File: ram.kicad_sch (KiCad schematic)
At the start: 26 parts, among them U16 SIMM, U17 74LS08, U18 74LS74, U19 74F00, U32 74LS139, U34 74LS244, U35 74LS244

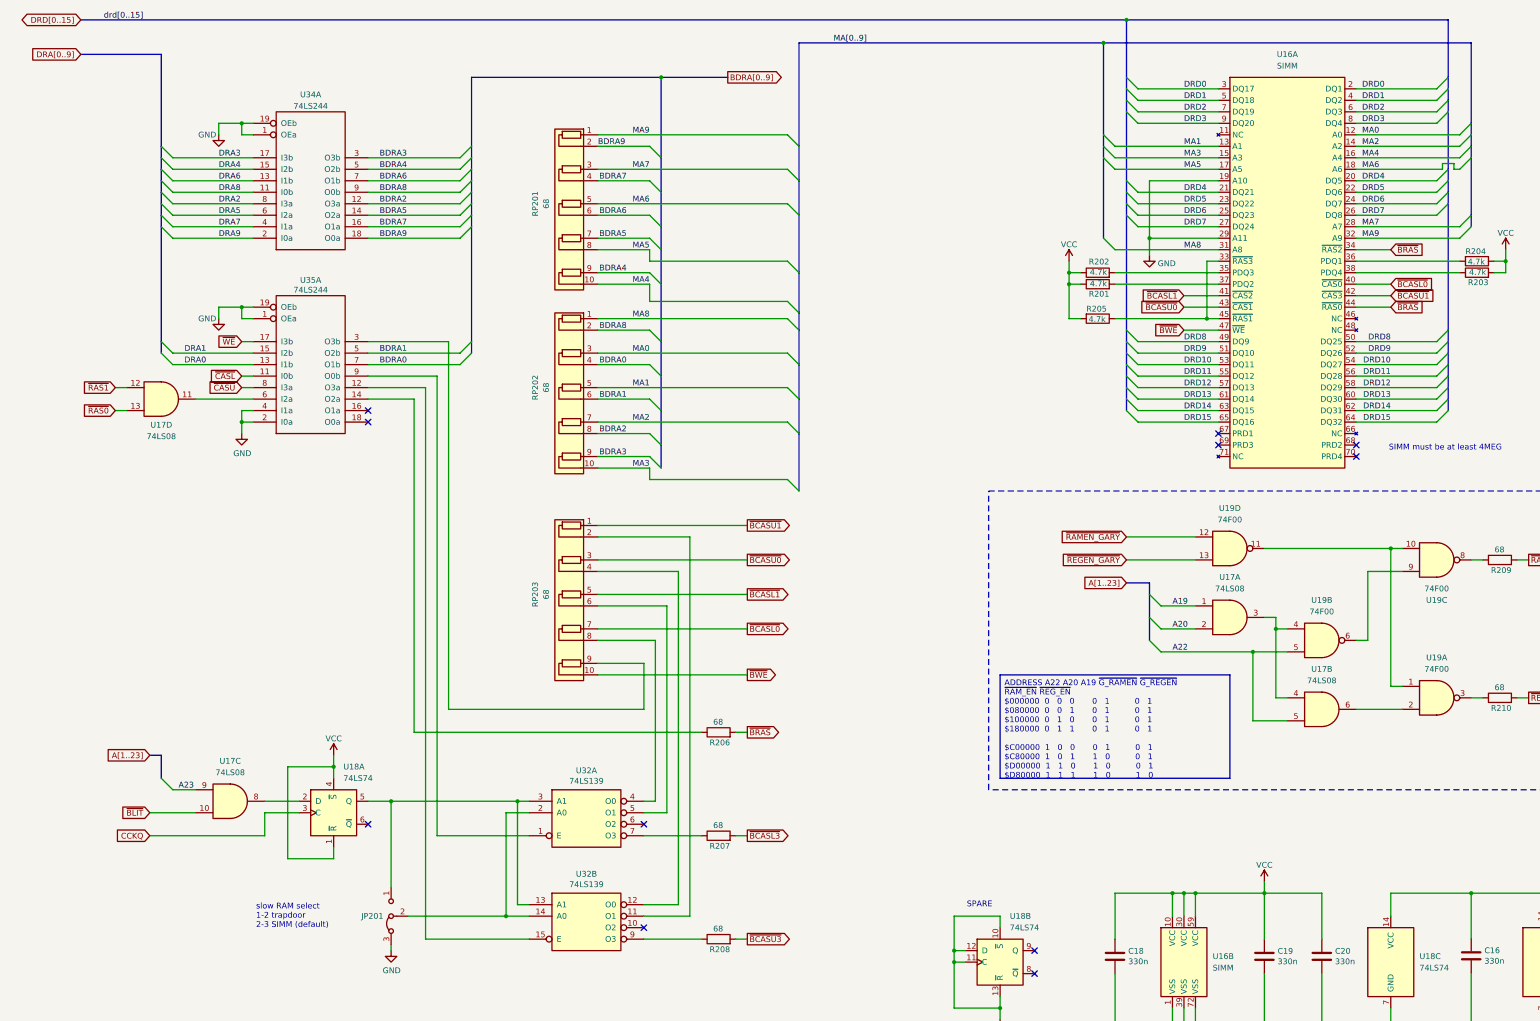
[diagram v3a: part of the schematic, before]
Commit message: routing SIMM
work in progress
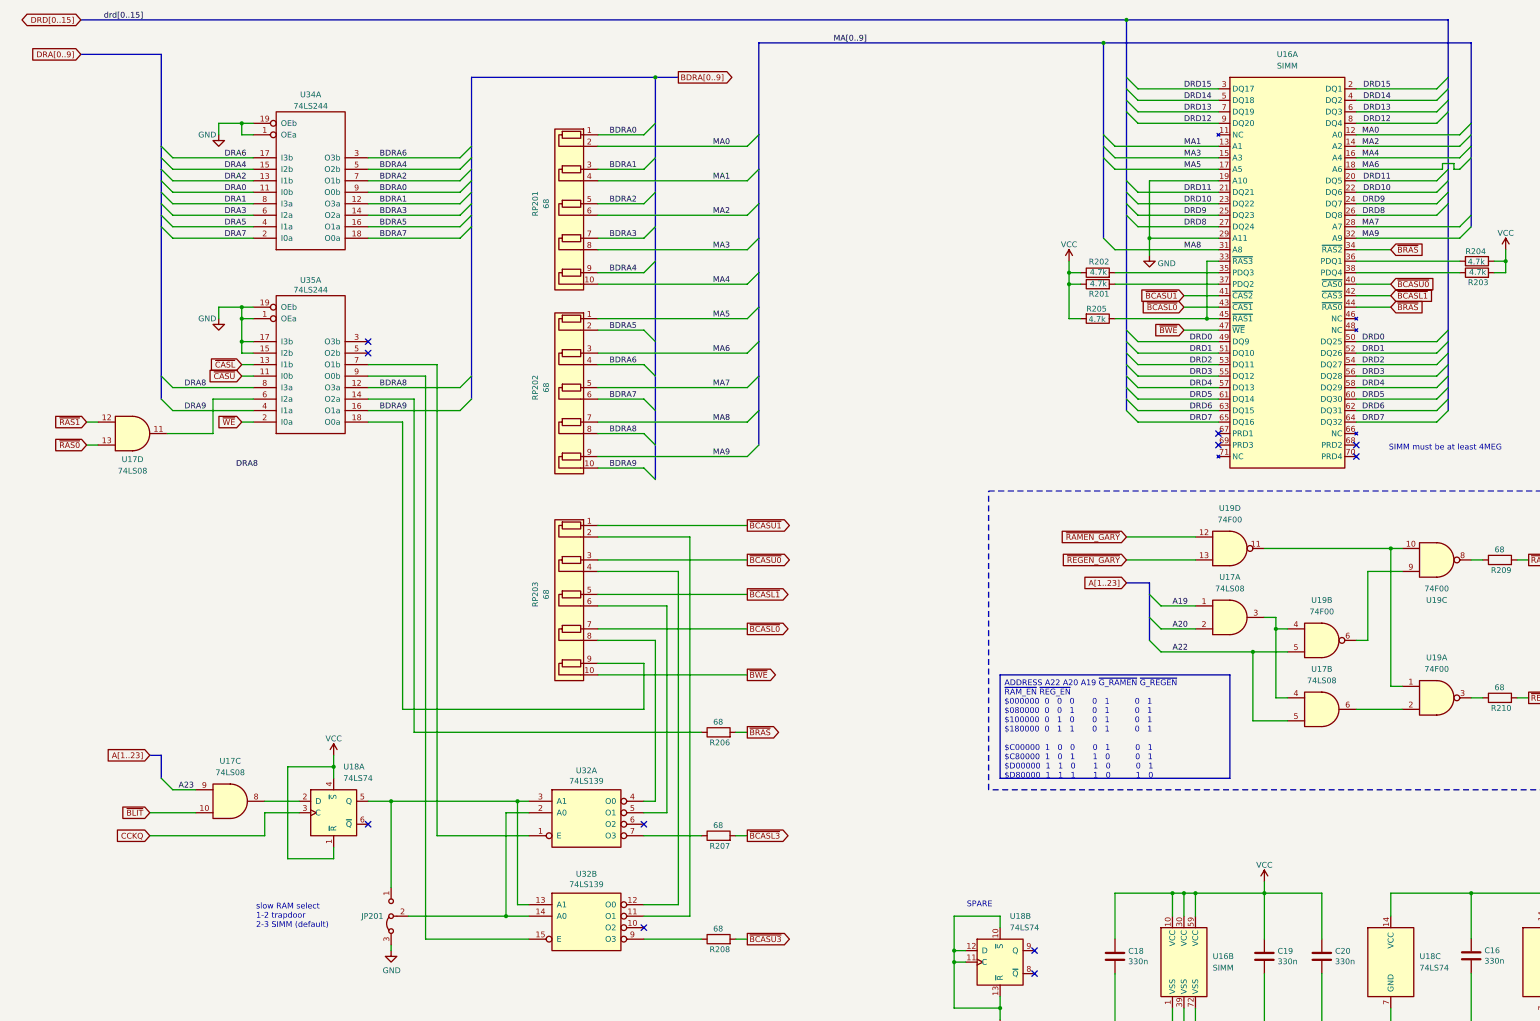
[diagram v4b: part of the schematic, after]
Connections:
- net BDRA0: now also RP201.1 (R1.1), U34.9 (O0b); no longer RP202.4 (R2.2), U35.7 (O1b)
- net BDRA1: now also RP201.3 (R2.1), U34.12 (O3a); no longer RP202.6 (R3.2), U35.5 (O2b)
- net BDRA2: now also RP201.5 (R3.1), U34.7 (O1b); no longer RP202.8 (R4.2), U34.12 (O3a)
- net BDRA3: now also RP201.7 (R4.1), U34.14 (O2a); no longer RP202.9 (R5.1), U34.3 (O3b)
- net BDRA5: now also RP202.2 (R1.2), U34.16 (O1a); no longer RP201.7 (R4.1), U34.14 (O2a)
- net BDRA6: now also RP202.4 (R2.2), U34.3 (O3b); no longer RP201.6 (R3.2), U34.7 (O1b)
- net BDRA7: now also RP202.6 (R3.2), U34.18 (O0a); no longer RP201.4 (R2.2), U34.16 (O1a)
- net BDRA8: now also RP202.8 (R4.2), U35.12 (O3a); no longer RP202.2 (R1.2), U34.9 (O0b)
- net BDRA9: now also RP202.10 (R5.2), U35.16 (O1a); no longer RP201.2 (R1.2), U34.18 (O0a)
- net DRA0: now also U34.11 (I0b); no longer U35.13 (I1b)
- net DRA1: now also U34.8 (I3a); no longer U35.15 (I2b)
- net DRA2: now also U34.13 (I1b); no longer U34.8 (I3a)
- net DRA3: now also U34.6 (I2a); no longer U34.17 (I3b)
- net DRA5: now also U34.4 (I1a); no longer U34.6 (I2a)
- net DRA6: now also U34.17 (I3b); no longer U34.13 (I1b)
- net DRA7: now also U34.2 (I0a); no longer U34.4 (I1a)
- net DRA8: now also U35.8 (I3a); no longer U34.11 (I0b)
- net DRA9: now also U35.4 (I1a); no longer U34.2 (I0a)
- net DRD0: now also U16.49 (DQ9), U16.50 (DQ25); no longer U16.2 (DQ1), U16.3 (DQ17)
- net DRD1: now also U16.51 (DQ10), U16.52 (DQ26); no longer U16.4 (DQ2), U16.5 (DQ18)
- net DRD10: now also U16.22 (DQ6), U16.23 (DQ22); no longer U16.53 (DQ11), U16.54 (DQ27)
- net DRD11: now also U16.20 (DQ5), U16.21 (DQ21); no longer U16.55 (DQ12), U16.56 (DQ28)
- net DRD12: now also U16.8 (DQ4), U16.9 (DQ20); no longer U16.57 (DQ13), U16.58 (DQ29)
- net DRD13: now also U16.6 (DQ3), U16.7 (DQ19); no longer U16.60 (DQ30), U16.61 (DQ14)
- net DRD14: now also U16.4 (DQ2), U16.5 (DQ18); no longer U16.62 (DQ31), U16.63 (DQ15)
- net DRD15: now also U16.2 (DQ1), U16.3 (DQ17); no longer U16.64 (DQ32), U16.65 (DQ16)
- net DRD2: now also U16.53 (DQ11), U16.54 (DQ27); no longer U16.6 (DQ3), U16.7 (DQ19)
- net DRD3: now also U16.55 (DQ12), U16.56 (DQ28); no longer U16.8 (DQ4), U16.9 (DQ20)
- net DRD4: now also U16.57 (DQ13), U16.58 (DQ29); no longer U16.20 (DQ5), U16.21 (DQ21)
- net DRD5: now also U16.60 (DQ30), U16.61 (DQ14); no longer U16.22 (DQ6), U16.23 (DQ22)
- net DRD6: now also U16.62 (DQ31), U16.63 (DQ15); no longer U16.24 (DQ7), U16.25 (DQ23)
- net DRD7: now also U16.64 (DQ32), U16.65 (DQ16); no longer U16.26 (DQ8), U16.27 (DQ24)
- net DRD8: now also U16.26 (DQ8), U16.27 (DQ24); no longer U16.49 (DQ9), U16.50 (DQ25)
- net DRD9: now also U16.24 (DQ7), U16.25 (DQ23); no longer U16.51 (DQ10), U16.52 (DQ26)
- net GND: now also U35.15 (I2b), U35.17 (I3b); no longer U35.2 (I0a), U35.4 (I1a)
- net MA0: now also RP201.2 (R1.2); no longer RP202.3 (R2.1)
- net MA1: now also RP201.4 (R2.2); no longer RP202.5 (R3.1)
- net MA2: now also RP201.6 (R3.2); no longer RP202.7 (R4.1)
- net MA3: now also RP201.8 (R4.2); no longer RP202.10 (R5.2)
- net MA5: now also RP202.1 (R1.1); no longer RP201.8 (R4.2)
- net MA6: now also RP202.3 (R2.1); no longer RP201.5 (R3.1)
- net MA7: now also RP202.5 (R3.1); no longer RP201.3 (R2.1)
- net MA8: now also RP202.7 (R4.1); no longer RP202.1 (R1.1)
- net MA9: now also RP202.9 (R5.1); no longer RP201.1 (R1.1)
- net ~{BCASL0}: now also U16.43 (~{CAS1}); no longer U16.40 (~{CAS0})
- net ~{BCASL1}: now also U16.42 (~{CAS3}); no longer U16.41 (~{CAS2})
- net ~{BCASU0}: now also U16.40 (~{CAS0}); no longer U16.43 (~{CAS1})
- net ~{BCASU1}: now also U16.41 (~{CAS2}); no longer U16.42 (~{CAS3})
- net ~{CASL}: now also U35.13 (I1b); no longer U35.11 (I0b)
- net ~{CASU}: now also U35.11 (I0b); no longer U35.8 (I3a)
- net ~{WE}: now also U35.2 (I0a); no longer U35.17 (I3b)
- net at U32.1 (E): now also U35.7 (O1b); no longer U35.9 (O0b)
- net at U32.15 (E): now also U35.9 (O0b); no longer U35.12 (O3a)
- net at U35.18 (O0a): now also RP203.9 (R5.1)
- net at U35.3 (O3b): no longer RP203.9 (R5.1)
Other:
- moved on the sheet: U17D

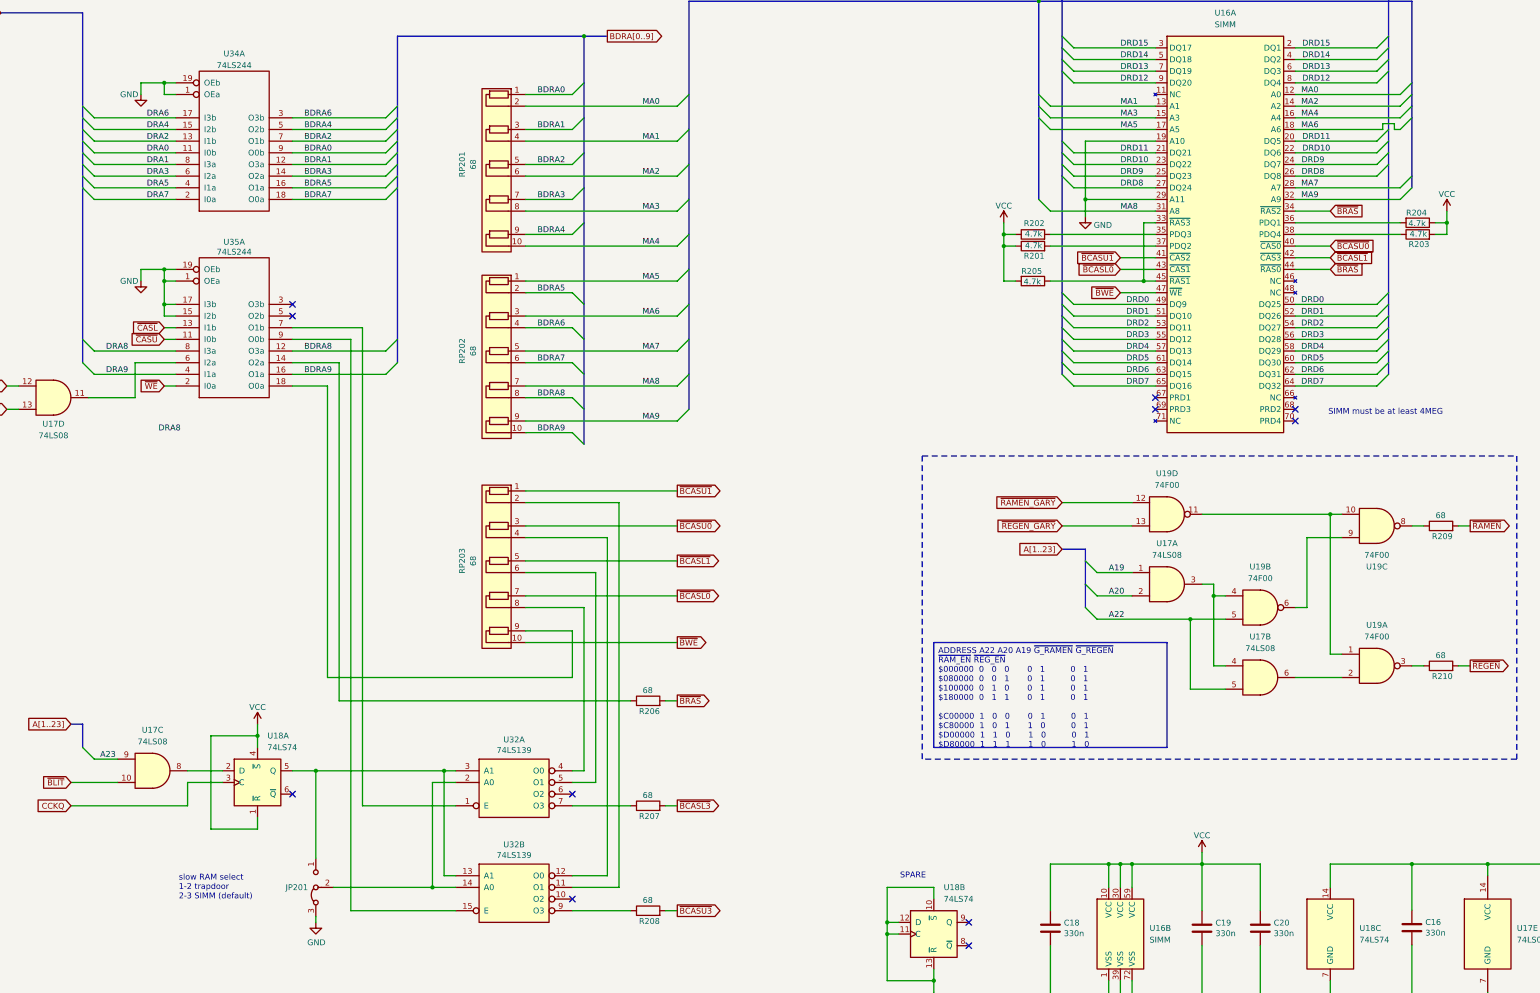
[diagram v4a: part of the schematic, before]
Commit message: changed wiring of pullups, simplified SIMM parity pullups
Routed more nets. Slowly getting there. WIP
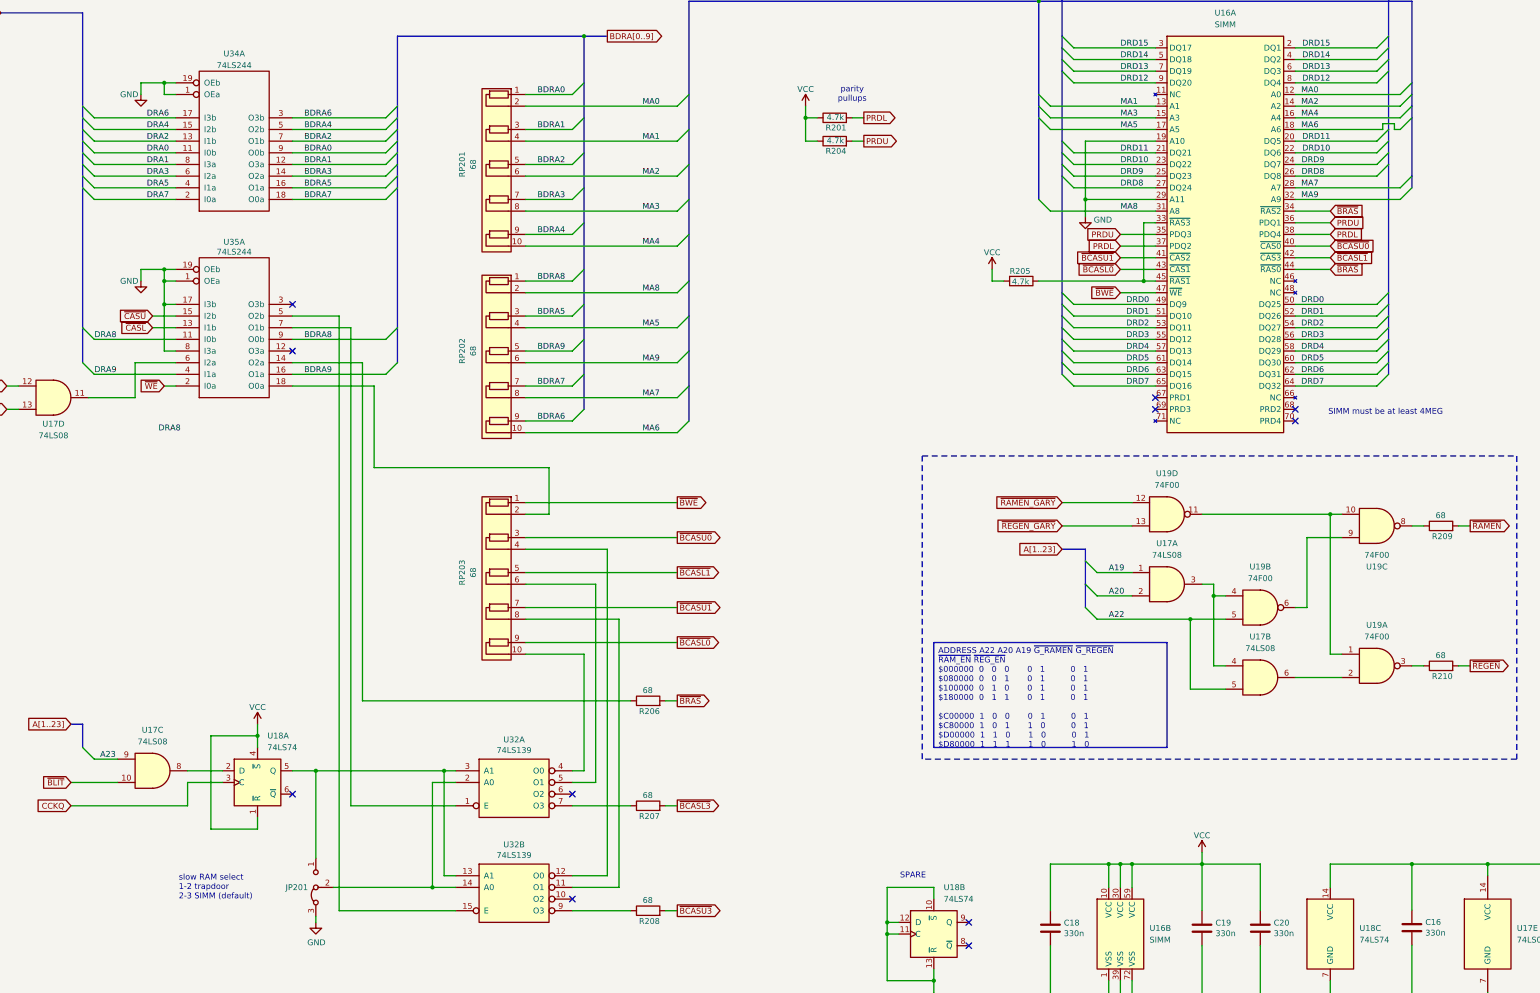
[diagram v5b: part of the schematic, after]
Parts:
- removed R202, R203: 4.7k, Raemixx500:R_Axial_DIN0309_L9.0mm_D3.2mm_P12.70mm_Horizontal, symbol Device:R
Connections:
- net BDRA5: now also RP202.3 (R2.1); no longer RP202.2 (R1.2)
- net BDRA6: now also RP202.9 (R5.1); no longer RP202.4 (R2.2)
- net BDRA7: now also RP202.7 (R4.1); no longer RP202.6 (R3.2)
- net BDRA8: now also RP202.1 (R1.1), U35.9 (O0b); no longer RP202.8 (R4.2), U35.12 (O3a)
- net BDRA9: now also RP202.5 (R3.1); no longer RP202.10 (R5.2)
- net DRA8: now also U35.11 (I0b); no longer U35.8 (I3a)
- net GND: now also U35.8 (I3a); no longer U35.15 (I2b)
- net MA5: now also RP202.4 (R2.2); no longer RP202.1 (R1.1)
- net MA6: now also RP202.10 (R5.2); no longer RP202.3 (R2.1)
- net MA7: now also RP202.8 (R4.2); no longer RP202.5 (R3.1)
- net MA8: now also RP202.2 (R1.2); no longer RP202.7 (R4.1)
- net MA9: now also RP202.6 (R3.2); no longer RP202.9 (R5.1)
- net ~{BCASL0}: now also RP203.9 (R5.1); no longer RP203.7 (R4.1)
- net ~{BCASU1}: now also RP203.7 (R4.1); no longer RP203.1 (R1.1)
- net ~{BWE}: now also RP203.1 (R1.1); no longer RP203.10 (R5.2)
- net ~{CASU}: now also U35.15 (I2b); no longer U35.11 (I0b)
- net at U32.4 (O0): now also RP203.10 (R5.2); no longer RP203.8 (R4.2)
- net at U32.11 (O1): now also RP203.8 (R4.2); no longer RP203.2 (R1.2)
- net at U32.15 (E): now also U35.5 (O2b); no longer U35.9 (O0b)
- net PRDL: now reaches R201.2, U16.37 (PDQ2)
- net PRDL: now also U16.38 (PDQ4)
- net PRDU: now reaches U16.35 (PDQ3)
- net PRDU: now also R204.2, U16.36 (PDQ1)
- net at U35.18 (O0a): now also RP203.2 (R1.2); no longer RP203.9 (R5.1)
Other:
- note added: "parity pullups"
- moved on the sheet: R201, R204, R205, RP203

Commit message: More work done, routing of SIMM module datapath almost done
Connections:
- net ~{BCASL1}: now also RP203.7 (R4.1); no longer RP203.5 (R3.1)
- net ~{BCASU1}: now also RP203.5 (R3.1); no longer RP203.7 (R4.1)
- net ~{BWE}: now also RP203.2 (R1.2); no longer RP203.1 (R1.1)
- net at U32.5 (O1): now also RP203.8 (R4.2); no longer RP203.6 (R3.2)
- net at U32.11 (O1): now also RP203.6 (R3.2); no longer RP203.8 (R4.2)
- net at U35.18 (O0a): now also RP203.1 (R1.1); no longer RP203.2 (R1.2)
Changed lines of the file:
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@@
 	(wire
 		(pts
-			(xy 162.56 215.9) (xy 162.56 157.48)
+			(xy 162.56 149.86) (xy 162.56 215.9)
 		)
 		(stroke
@@
 	(wire
 		(pts
-			(xy 147.32 134.62) (xy 147.32 124.46)
-		)
-		(stroke
-			(width 0)
-			(type default)
-		)
-	)
-	(wire
-		(pts
 			(xy 57.15 109.22) (xy 46.99 109.22)
 		)
@@
 	(wire
 		(pts
-			(xy 142.24 157.48) (xy 162.56 157.48)
-		)
-		(stroke
-			(width 0)
-			(type default)
-		)
-	)
-	(wire
-		(pts
 			(xy 261.62 55.88) (xy 279.4 55.88)
 		)
@@
 	(wire
 		(pts
-			(xy 142.24 132.08) (xy 175.26 132.08)
-		)
-		(stroke
-			(width 0)
-			(type default)
-		)
-	)
-	(wire
-		(pts
 			(xy 96.52 222.25) (xy 96.52 223.52)
 		)
@@
 	(wire
 		(pts
-			(xy 142.24 134.62) (xy 147.32 134.62)
+			(xy 269.24 241.3) (xy 271.78 241.3)
 		)
 		(stroke
@@
 	(wire
 		(pts
-			(xy 269.24 241.3) (xy 271.78 241.3)
+			(xy 203.2 45.72) (xy 203.2 48.26)
 		)
 		(stroke
@@
 	(wire
 		(pts
-			(xy 203.2 45.72) (xy 203.2 48.26)
+			(xy 152.4 198.12) (xy 165.1 198.12)
 		)
 		(stroke
@@
 		)
 	)
-	(wire
+	(bus
 		(pts
-			(xy 152.4 198.12) (xy 165.1 198.12)
+			(xy 177.8 66.04) (xy 177.8 73.66)
 		)
 		(stroke
@@
 		)
 	)
-	(bus
+	(wire
 		(pts
-			(xy 177.8 66.04) (xy 177.8 73.66)
+			(xy 142.24 134.62) (xy 175.26 134.62)
 		)
 		(stroke
@@
 		)
 	)
+	(wire
+		(pts
+			(xy 157.48 157.48) (xy 157.48 193.04)
+		)
+		(stroke
+			(width 0)
+			(type default)
+		)
+	)
 	(bus
 		(pts
@@
 	(wire
 		(pts
-			(xy 157.48 149.86) (xy 142.24 149.86)
-		)
-		(stroke
-			(width 0)
-			(type default)
-		)
-	)
-	(wire
-		(pts
 			(xy 142.24 68.58) (xy 175.26 68.58)
 		)
@@
 		)
 	)
+	(wire
+		(pts
+			(xy 142.24 149.86) (xy 162.56 149.86)
+		)
+		(stroke
+			(width 0)
+			(type default)
+		)
+	)
 	(bus
 		(pts
@@
 		)
 	)
+	(wire
+		(pts
+			(xy 147.32 132.08) (xy 147.32 124.46)
+		)
+		(stroke
+			(width 0)
+			(type default)
+		)
+	)
 	(bus
 		(pts
@@
 	(wire
 		(pts
+			(xy 142.24 157.48) (xy 157.48 157.48)
+		)
+		(stroke
+			(width 0)
+			(type default)
+		)
+	)
+	(wire
+		(pts
 			(xy 220.98 226.06) (xy 220.98 236.22)
 		)
@@
 	(wire
 		(pts
-			(xy 157.48 149.86) (xy 157.48 193.04)
-		)
-		(stroke
-			(width 0)
-			(type default)
-		)
-	)
-	(wire
-		(pts
 			(xy 351.79 210.82) (xy 370.84 210.82)
 		)
@@
 	(wire
 		(pts
+			(xy 142.24 132.08) (xy 147.32 132.08)
+		)
+		(stroke
+			(width 0)
+			(type default)
+		)
+	)
+	(wire
+		(pts
 			(xy 60.96 93.98) (xy 66.04 93.98)
 		)
@@
 	(global_label "~{BCASL1}"
 		(shape output)
-		(at 175.26 147.32 0)
+		(at 175.26 154.94 0)
 		(fields_autoplaced yes)
 		(effects
@@
 		)
 		(property "Intersheetrefs" "${INTERSHEET_REFS}"
-			(at 184.6667 147.32 0)
+			(at 184.6667 154.94 0)
 			(effects
 				(font
@@
 	(global_label "~{BWE}"
 		(shape output)
-		(at 175.26 132.08 0)
+		(at 175.26 134.62 0)
 		(fields_autoplaced yes)
 		(effects
@@
 		)
 		(property "Intersheetrefs" "${INTERSHEET_REFS}"
-			(at 181.4614 132.08 0)
+			(at 181.4614 134.62 0)
 			(effects
 				(font
@@
 	(global_label "~{BCASU1}"
 		(shape output)
-		(at 175.26 154.94 0)
+		(at 175.26 147.32 0)
 		(fields_autoplaced yes)
 		(effects
@@
 		)
 		(property "Intersheetrefs" "${INTERSHEET_REFS}"
-			(at 184.9691 154.94 0)
+			(at 184.9691 147.32 0)
 			(effects
 				(font
